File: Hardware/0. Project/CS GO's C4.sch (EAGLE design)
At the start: 44 parts, among them CN1 CELL--PHMC4-02, CN2 ICSP, CN4 TERMINAL-BLOCK-2P-5MM, CN5 TERMINAL-BLOCK-2P-5MM, Q1 NPN-BC817, Q3 N-FET-ENHANCEMENT-SQ2310, SW1 SPST-LATCH-PHMC4-02, U1 1117-3.3V, U4 PCF8574DW, U6 ATMEGA328P-PU

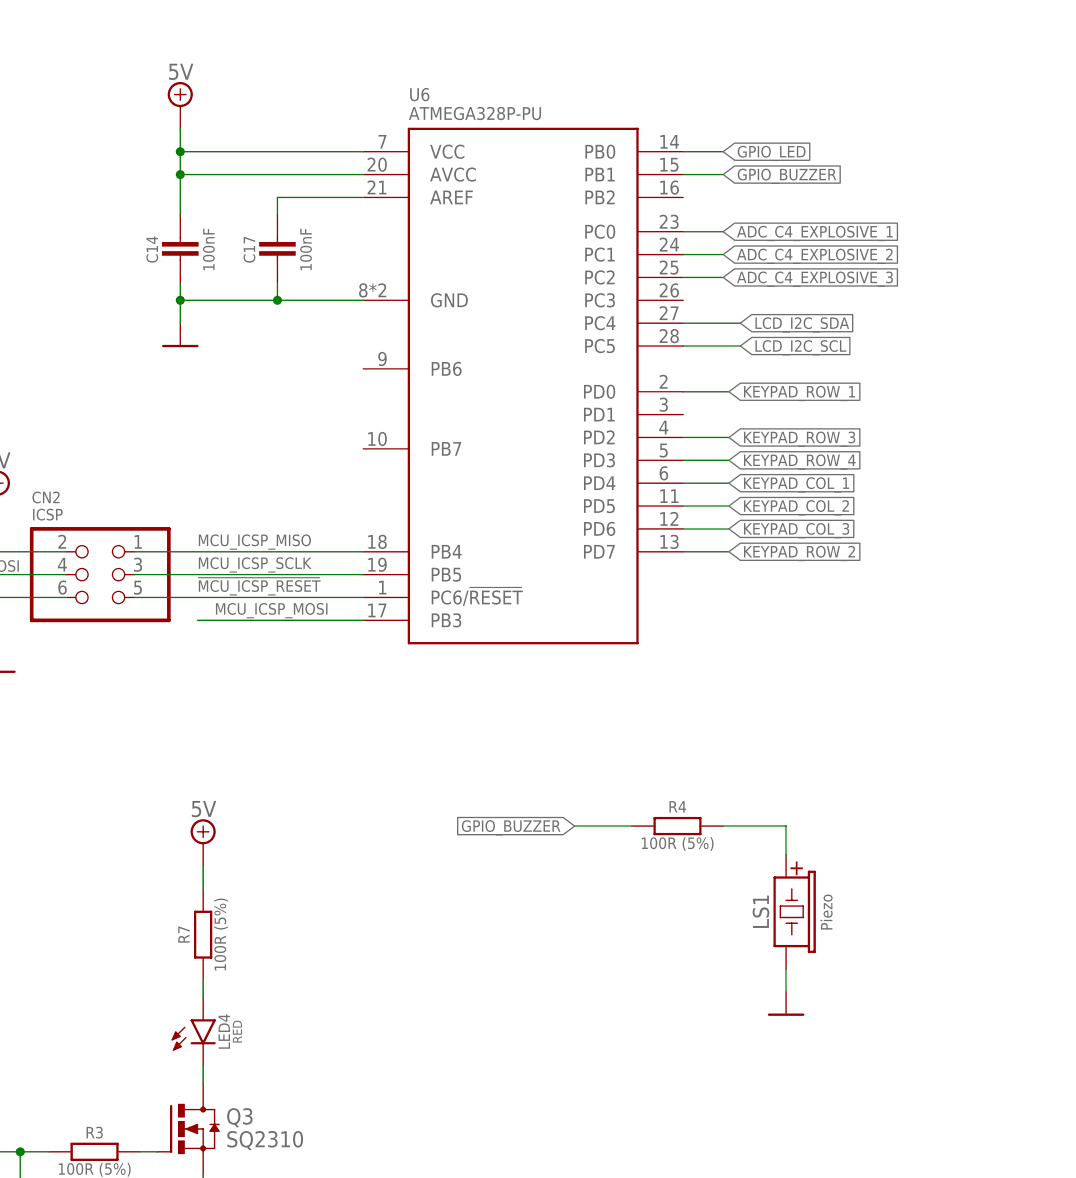
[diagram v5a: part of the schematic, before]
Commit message: added external crystal & buzzer controlled by ac signal
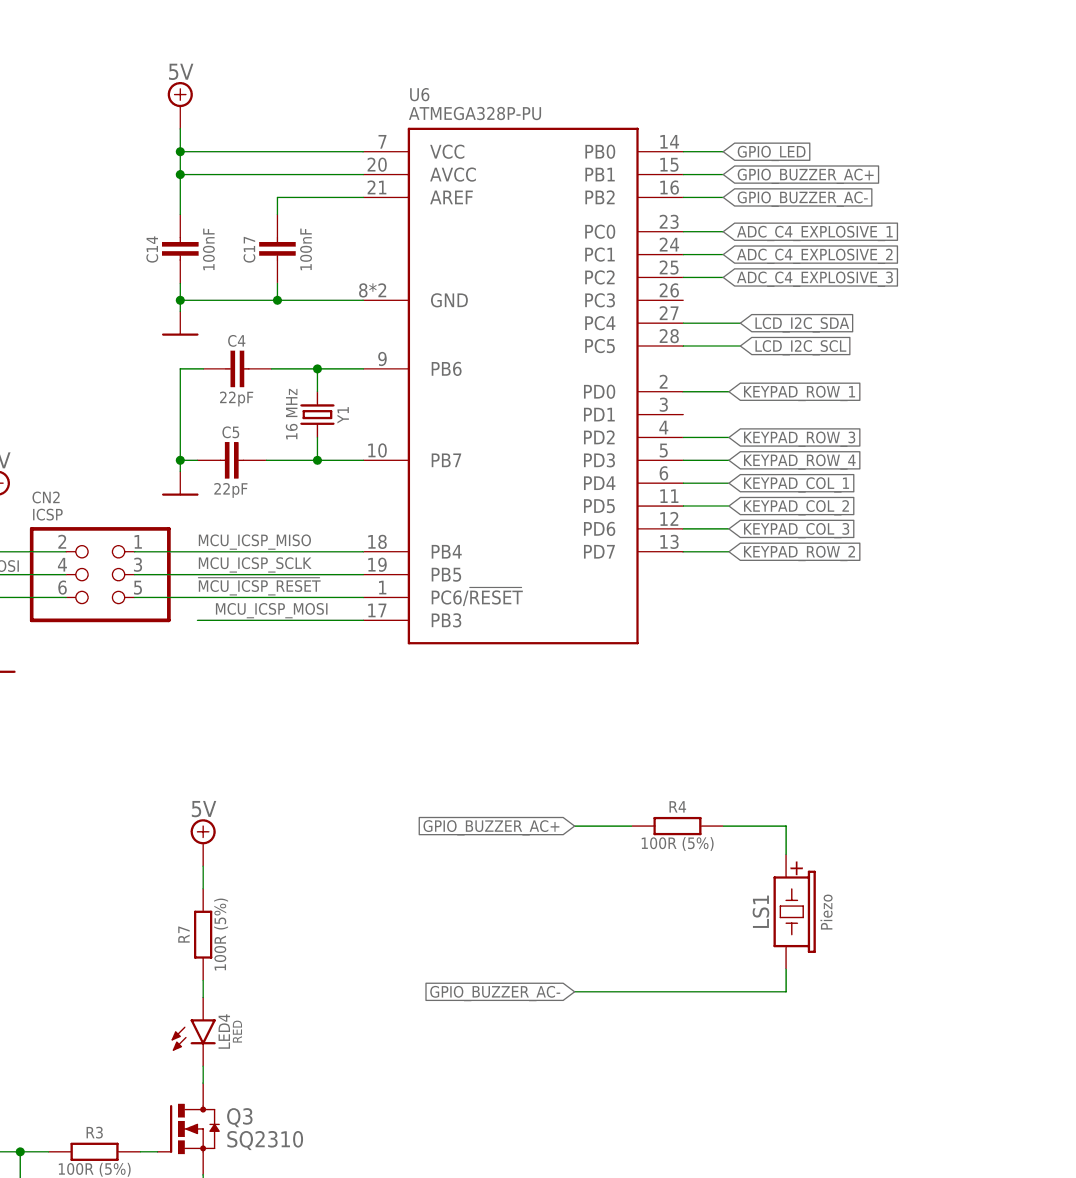
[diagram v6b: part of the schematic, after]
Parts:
- added C4, C5: 22pF, My-RLC:C_0603
- added Y1: 16 MHz, My-Crystals:OSC-25MHZ
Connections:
- net GPIO_BUZZER renamed GPIO_BUZZER_AC+
- new net GPIO_BUZZER_AC-: LS1.-, U6.PB2
- new net N$12: C4.1, U6.PB6, Y1.1
- new net N$6: C5.1, U6.PB7, Y1.2
- net 0V: now also C4.2, C5.2; no longer LS1.-
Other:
- note removed: "** needs custom bootloader ** checks Firmware\\CUSTOM\\README.txt"
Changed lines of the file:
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@@
 <attribute name="AUTHOR" value="Tiago Silva"/>
 <attribute name="SOURCE" value="github.com/TiagoPaulaSilva/CS-GO-s-C4"/>
-<attribute name="VERSION" value="1.5"/>
+<attribute name="VERSION" value="1.6"/>
 </attributes>
 <variantdefs>
@@
 <part name="SUPPLY24" library="My-Supply" library_urn="urn:adsk.eagle:library:35531236" deviceset="5V" device=""/>
 <part name="R7" library="My-RLC" library_urn="urn:adsk.eagle:library:35509816" deviceset="R_" device="0603" package3d_urn="urn:adsk.eagle:package:35509946/1" value="100R (5%)"/>
-<part name="SUPPLY25" library="My-Supply" library_urn="urn:adsk.eagle:library:35531236" deviceset="0V" device=""/>
+<part name="Y1" library="My-Crystals" library_urn="urn:adsk.eagle:library:35670754" deviceset="OSC-" device="25MHZ" package3d_urn="urn:adsk.eagle:package:35670742/3" value="16 MHz"/>
+<part name="C4" library="My-RLC" library_urn="urn:adsk.eagle:library:35509816" deviceset="C_" device="0603" package3d_urn="urn:adsk.eagle:package:35509984/1" value="22pF"/>
+<part name="C5" library="My-RLC" library_urn="urn:adsk.eagle:library:35509816" deviceset="C_" device="0603" package3d_urn="urn:adsk.eagle:package:35509984/1" value="22pF"/>
+<part name="SUPPLY27" library="My-Supply" library_urn="urn:adsk.eagle:library:35531236" deviceset="0V" device=""/>
 </parts>
 <sheets>
@@
 <text x="325.755" y="65.0875" size="1.27" layer="135" rot="R270" align="center" grouprefs="C4_SHELLS_DETECTION">C4 SHELL</text>
 <text x="337.185" y="65.0875" size="1.27" layer="135" rot="R270" align="center" grouprefs="C4_SHELLS_DETECTION">C4 SHELL</text>
-<text x="120.65" y="104.775" size="1.778" layer="140" align="center" grouprefs="MICROCONTROLLER">** needs custom bootloader **
-checks Firmware\\CUSTOM\\README.txt</text>
 </plain>
 <instances>
@@
 <attribute name="VALUE" x="85.09" y="152.9334" size="1.27" layer="96" rot="R90" align="center"/>
 </instance>
-<instance part="SUPPLY5" gate="G$1" x="81.915" y="142.24" smashed="yes" grouprefs="MICROCONTROLLER"/>
+<instance part="SUPPLY5" gate="G$1" x="81.915" y="143.51" smashed="yes" grouprefs="MICROCONTROLLER"/>
 <instance part="CN2" gate="A" x="73.025" y="116.84" smashed="yes" rot="MR0" grouprefs="MICROCONTROLLER">
 <attribute name="NAME" x="65.405" y="124.7775" size="1.27" layer="95"/>
@@
 <attribute name="VALUE" x="86.36" y="76.835" size="1.27" layer="96" rot="R90" align="center"/>
 </instance>
-<instance part="SUPPLY25" gate="G$1" x="149.225" y="67.945" smashed="yes" grouprefs="BUZZER"/>
+<instance part="Y1" gate="U1" x="97.155" y="134.62" smashed="yes" rot="R270">
+<attribute name="NAME" x="100.0125" y="134.62" size="1.27" layer="95" rot="R270" align="center"/>
+<attribute name="VALUE" x="94.2975" y="134.62" size="1.27" layer="96" rot="R270" align="center"/>
+</instance>
+<instance part="C4" gate="G$1" x="89.535" y="139.7" smashed="yes" rot="R270">
+<attribute name="NAME" x="88.1888" y="142.8115" size="1.27" layer="95" align="center"/>
+<attribute name="VALUE" x="88.1634" y="136.525" size="1.27" layer="96" align="center"/>
+</instance>
+<instance part="C5" gate="G$1" x="88.9" y="129.54" smashed="yes" rot="R270">
+<attribute name="NAME" x="87.5538" y="132.6515" size="1.27" layer="95" align="center"/>
+<attribute name="VALUE" x="87.5284" y="126.365" size="1.27" layer="96" align="center"/>
+</instance>
+<instance part="SUPPLY27" gate="G$1" x="81.915" y="125.73" smashed="yes"/>
 </instances>
 <busses>
@@
 <wire x1="81.915" y1="147.32" x2="81.915" y2="149.225" width="0.1524" layer="91" grouprefs="MICROCONTROLLER"/>
 <pinref part="SUPPLY5" gate="G$1" pin="0V"/>
-<wire x1="81.915" y1="144.78" x2="81.915" y2="147.32" width="0.1524" layer="91" grouprefs="MICROCONTROLLER"/>
+<wire x1="81.915" y1="146.05" x2="81.915" y2="147.32" width="0.1524" layer="91" grouprefs="MICROCONTROLLER"/>
 <junction x="81.915" y="147.32" grouprefs="MICROCONTROLLER"/>
 <pinref part="C17" gate="G$1" pin="2"/>
@@
 </segment>
 <segment>
-<pinref part="LS1" gate="G$1" pin="-"/>
-<pinref part="SUPPLY25" gate="G$1" pin="0V"/>
-<wire x1="149.225" y1="70.485" x2="149.225" y2="73.025" width="0.1524" layer="91" grouprefs="BUZZER"/>
+<pinref part="C5" gate="G$1" pin="2"/>
+<pinref part="SUPPLY27" gate="G$1" pin="0V"/>
+<wire x1="83.82" y1="129.54" x2="81.915" y2="129.54" width="0.1524" layer="91"/>
+<wire x1="81.915" y1="129.54" x2="81.915" y2="128.27" width="0.1524" layer="91"/>
+<pinref part="C4" gate="G$1" pin="2"/>
+<wire x1="84.455" y1="139.7" x2="81.915" y2="139.7" width="0.1524" layer="91"/>
+<wire x1="81.915" y1="139.7" x2="81.915" y2="129.54" width="0.1524" layer="91"/>
+<junction x="81.915" y="129.54"/>
 </segment>
 </net>
@@
 </segment>
 </net>
-<net name="GPIO_BUZZER" class="0">
+<net name="GPIO_BUZZER_AC+" class="0">
 <segment>
 <label x="142.24" y="161.29" size="1.27" layer="95" xref="yes" grouprefs="MICROCONTROLLER"/>
@@
 </segment>
 </net>
+<net name="GPIO_BUZZER_AC-" class="0">
+<segment>
+<pinref part="U6" gate="G$1" pin="PB2"/>
+<wire x1="137.795" y1="158.75" x2="142.24" y2="158.75" width="0.1524" layer="91"/>
+<label x="142.24" y="158.75" size="1.27" layer="95" xref="yes"/>
+</segment>
+<segment>
+<pinref part="LS1" gate="G$1" pin="-"/>
+<wire x1="149.225" y1="73.025" x2="149.225" y2="70.485" width="0.1524" layer="91"/>
+<wire x1="149.225" y1="70.485" x2="125.73" y2="70.485" width="0.1524" layer="91"/>
+<label x="125.73" y="70.485" size="1.27" layer="95" rot="R180" xref="yes"/>
+</segment>
+</net>
+<net name="N$12" class="0">
+<segment>
+<pinref part="U6" gate="G$1" pin="PB6"/>
+<wire x1="102.235" y1="139.7" x2="97.155" y2="139.7" width="0.1524" layer="91"/>
+<pinref part="Y1" gate="U1" pin="1"/>
+<wire x1="97.155" y1="137.16" x2="97.155" y2="139.7" width="0.1524" layer="91"/>
+<pinref part="C4" gate="G$1" pin="1"/>
+<wire x1="92.075" y1="139.7" x2="97.155" y2="139.7" width="0.1524" layer="91"/>
+<junction x="97.155" y="139.7"/>
+</segment>
+</net>
+<net name="N$6" class="0">
+<segment>
+<pinref part="Y1" gate="U1" pin="2"/>
+<pinref part="U6" gate="G$1" pin="PB7"/>
+<wire x1="97.155" y1="132.08" x2="97.155" y2="129.54" width="0.1524" layer="91"/>
+<pinref part="C5" gate="G$1" pin="1"/>
+<wire x1="97.155" y1="129.54" x2="102.235" y2="129.54" width="0.1524" layer="91"/>
+<wire x1="91.44" y1="129.54" x2="97.155" y2="129.54" width="0.1524" layer="91"/>
+<junction x="97.155" y="129.54"/>
+</segment>
+</net>
 </nets>
 </sheet>
@@
 </drawing>
 <compatibility>
-<note version="6.3" minversion="6.2.2" severity="warning">
-Since Version 6.2.2 text objects can contain more than one line,
-which will not be processed correctly with this version.
-</note>
 <note version="8.2" severity="warning">
 Since Version 8.2, EAGLE supports online libraries. The ids

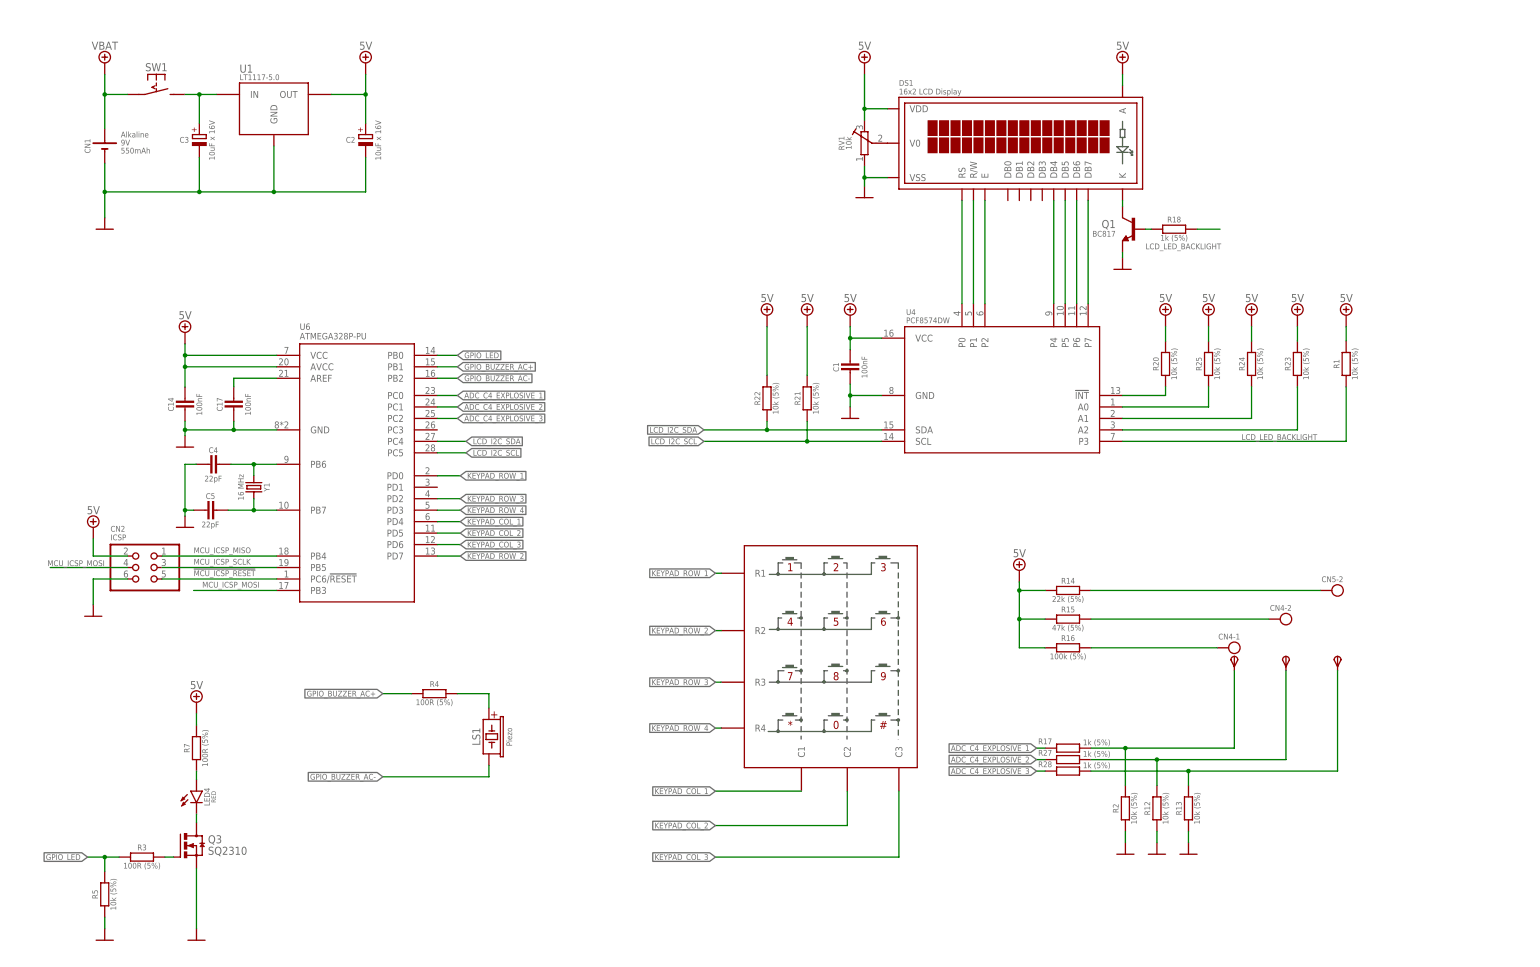
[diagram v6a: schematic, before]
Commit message: added pins to control lcd brightness
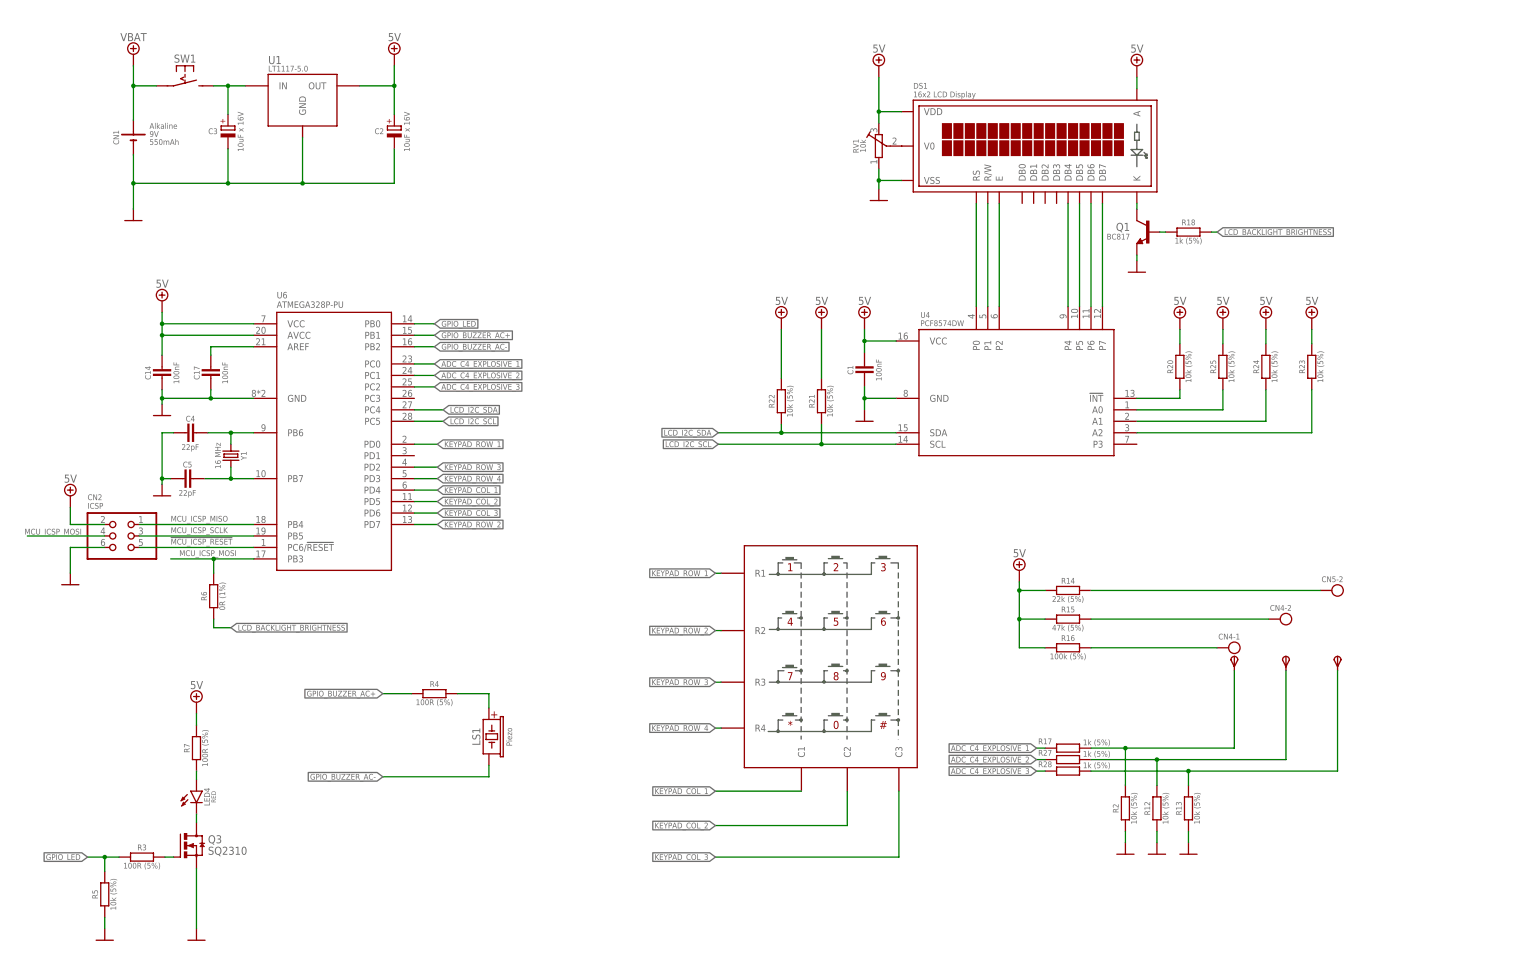
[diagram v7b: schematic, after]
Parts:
- removed R1: 10k (5%), My-RLC:R_0603
- added R6: 0R (1%), My-RLC:R_0603
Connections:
- removed net LCD_LED_BACKLIGHT: R1.1, R18.1, U4.P3
- new net LCD_BACKLIGHT_BRIGHTNESS: R18.1, R6.1
- net 5.0V: no longer R1.2
- net MCU_ICSP_MOSI: now also R6.2
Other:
- moved on the sheet: C1, C14, C17, C2, C3, C4, C5, CN1, CN2, DS1, Q1, R18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
